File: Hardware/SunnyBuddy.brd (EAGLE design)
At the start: 47 x 47 mm, 38 parts, among them J1 5.5x2.1mm Barrel, J2 POWER_JACKPTH, J5 M02PTH, J6 M023.5MM, J7 M023.5MM, J8 M023.5MM, U1 LT3652

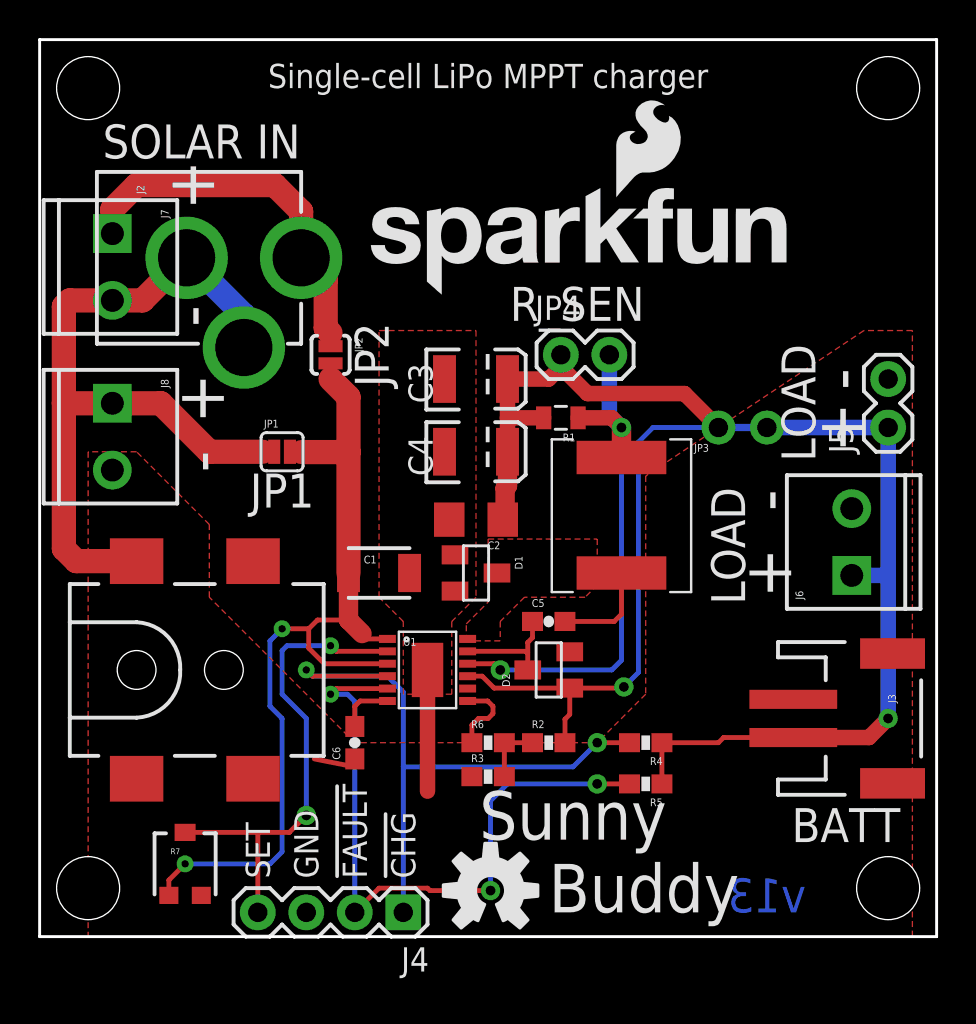
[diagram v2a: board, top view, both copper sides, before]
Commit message: added board fiducials
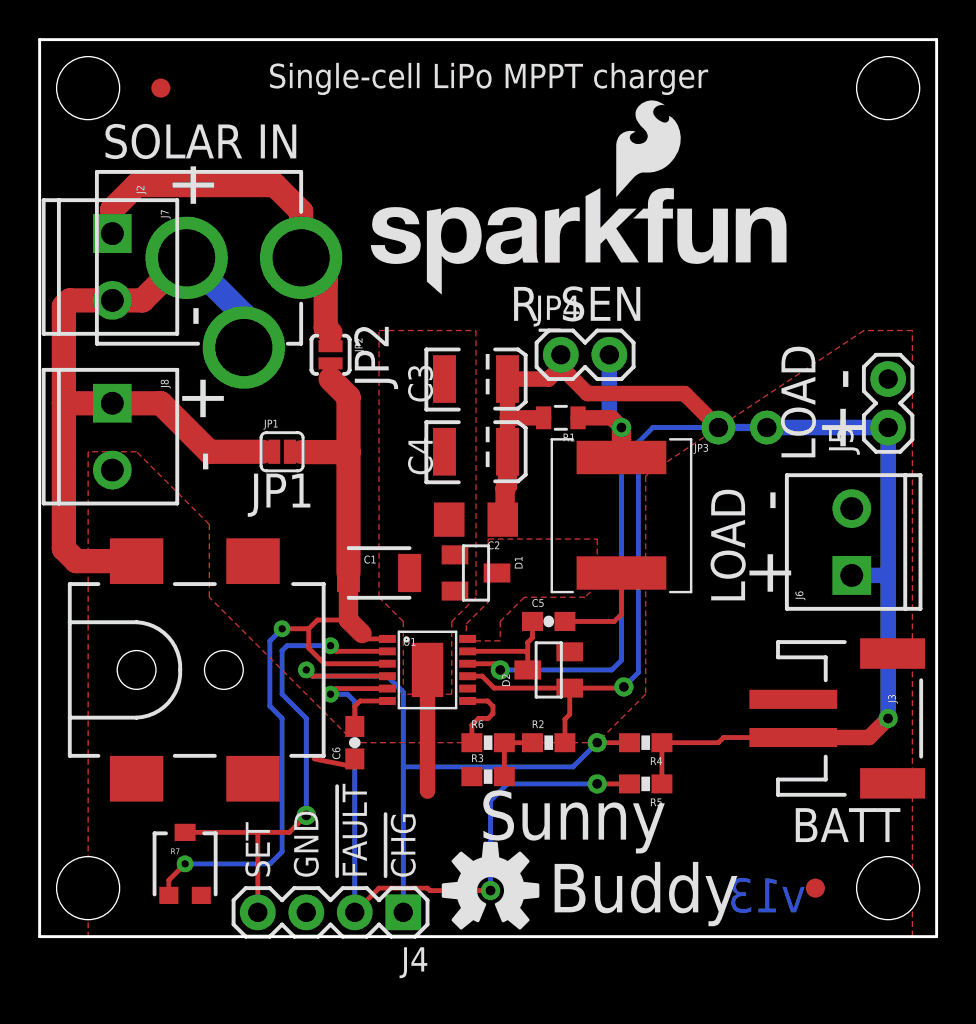
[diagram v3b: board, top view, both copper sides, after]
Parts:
- added FID1, FID2: FIDUCIAL1X2, SparkFun-Aesthetics:FIDUCIAL-1X2
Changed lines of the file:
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@@
 <?xml version="1.0" encoding="utf-8"?>
 <!DOCTYPE eagle SYSTEM "eagle.dtd">
-<eagle version="6.5.0">
+<eagle version="6.6.0">
 <drawing>
 <settings>
@@
 <setting verticaltext="up"/>
 </settings>
-<grid distance="0.05" unitdist="inch" unit="inch" style="lines" multiple="1" display="yes" altdistance="0.005" altunitdist="inch" altunit="inch"/>
+<grid distance="0.05" unitdist="inch" unit="inch" style="lines" multiple="1" display="yes" altdistance="0.01" altunitdist="inch" altunit="inch"/>
 <layers>
-<layer number="1" name="Top" color="4" fill="1" visible="no" active="yes"/>
-<layer number="2" name="Route2" color="1" fill="3" visible="no" active="yes"/>
-<layer number="15" name="Route15" color="4" fill="6" visible="no" active="yes"/>
+<layer number="1" name="Top" color="4" fill="1" visible="yes" active="yes"/>
+<layer number="2" name="Route2" color="1" fill="3" visible="yes" active="yes"/>
+<layer number="15" name="Route15" color="4" fill="6" visible="yes" active="yes"/>
 <layer number="16" name="Bottom" color="1" fill="1" visible="yes" active="yes"/>
 <layer number="17" name="Pads" color="2" fill="1" visible="yes" active="yes"/>
 <layer number="18" name="Vias" color="2" fill="1" visible="yes" active="yes"/>
 <layer number="19" name="Unrouted" color="6" fill="1" visible="yes" active="yes"/>
-<layer number="20" name="Dimension" color="15" fill="1" visible="yes" active="yes"/>
-<layer number="21" name="tPlace" color="16" fill="1" visible="no" active="yes"/>
-<layer number="22" name="bPlace" color="14" fill="1" visible="yes" active="yes"/>
-<layer number="23" name="tOrigins" color="15" fill="1" visible="no" active="yes"/>
+<layer number="20" name="Dimension" color="6" fill="1" visible="yes" active="yes"/>
+<layer number="21" name="tPlace" color="6" fill="1" visible="yes" active="yes"/>
+<layer number="22" name="bPlace" color="6" fill="1" visible="yes" active="yes"/>
+<layer number="23" name="tOrigins" color="15" fill="1" visible="yes" active="yes"/>
 <layer number="24" name="bOrigins" color="15" fill="1" visible="yes" active="yes"/>
-<layer number="25" name="tNames" color="7" fill="1" visible="no" active="yes"/>
-<layer number="26" name="bNames" color="7" fill="1" visible="no" active="yes"/>
-<layer number="27" name="tValues" color="7" fill="1" visible="no" active="yes"/>
-<layer number="28" name="bValues" color="7" fill="1" visible="no" active="yes"/>
-<layer number="29" name="tStop" color="7" fill="3" visible="no" active="yes"/>
-<layer number="30" name="bStop" color="7" fill="6" visible="no" active="yes"/>
-<layer number="31" name="tCream" color="7" fill="4" visible="no" active="yes"/>
-<layer number="32" name="bCream" color="7" fill="5" visible="no" active="yes"/>
-<layer number="39" name="tKeepout" color="4" fill="11" visible="no" active="yes"/>
-<layer number="40" name="bKeepout" color="1" fill="11" visible="no" active="yes"/>
-<layer number="41" name="tRestrict" color="4" fill="10" visible="no" active="yes"/>
-<layer number="42" name="bRestrict" color="1" fill="10" visible="no" active="yes"/>
-<layer number="43" name="vRestrict" color="2" fill="10" visible="no" active="yes"/>
-<layer number="44" name="Drills" color="7" fill="1" visible="no" active="yes"/>
-<layer number="45" name="Holes" color="7" fill="1" visible="no" active="yes"/>
-<layer number="46" name="Milling" color="3" fill="1" visible="no" active="yes"/>
-<layer number="51" name="tDocu" color="6" fill="1" visible="no" active="yes"/>
-<layer number="52" name="bDocu" color="7" fill="1" visible="no" active="yes"/>
+<layer number="25" name="tNames" color="7" fill="1" visible="yes" active="yes"/>
+<layer number="26" name="bNames" color="7" fill="1" visible="yes" active="yes"/>
+<layer number="27" name="tValues" color="7" fill="1" visible="yes" active="yes"/>
+<layer number="28" name="bValues" color="7" fill="1" visible="yes" active="yes"/>
+<layer number="29" name="tStop" color="7" fill="3" visible="yes" active="yes"/>
+<layer number="30" name="bStop" color="7" fill="6" visible="yes" active="yes"/>
+<layer number="31" name="tCream" color="7" fill="4" visible="yes" active="yes"/>
+<layer number="32" name="bCream" color="7" fill="5" visible="yes" active="yes"/>
+<layer number="39" name="tKeepout" color="4" fill="11" visible="yes" active="yes"/>
+<layer number="40" name="bKeepout" color="1" fill="11" visible="yes" active="yes"/>
+<layer number="41" name="tRestrict" color="4" fill="10" visible="yes" active="yes"/>
+<layer number="42" name="bRestrict" color="1" fill="10" visible="yes" active="yes"/>
+<layer number="43" name="vRestrict" color="2" fill="10" visible="yes" active="yes"/>
+<layer number="44" name="Drills" color="7" fill="1" visible="yes" active="yes"/>
+<layer number="45" name="Holes" color="7" fill="1" visible="yes" active="yes"/>
+<layer number="46" name="Milling" color="3" fill="1" visible="yes" active="yes"/>
+<layer number="51" name="tDocu" color="6" fill="1" visible="yes" active="yes"/>
+<layer number="52" name="bDocu" color="7" fill="1" visible="yes" active="yes"/>
 <layer number="3" name="Route3" color="4" fill="3" visible="no" active="no"/>
 <layer number="4" name="Route4" color="1" fill="4" visible="no" active="no"/>
@@
 <element name="LOGO3" library="SparkFun-Aesthetics" package="OSHW-LOGO-S" value="OSHW-LOGOS" x="2.54" y="7.62" rot="MR0"/>
 <element name="LOGO4" library="SparkFun-Aesthetics" package="SFE_LOGO_NAME_FLAME_.3" value="SFE_LOGO_NAME_FLAME.3_INCH" x="40.64" y="15.24" rot="MR0"/>
+<element name="FID1" library="SparkFun-Aesthetics" package="FIDUCIAL-1X2" value="FIDUCIAL1X2" x="6.35" y="44.45"/>
+<element name="FID2" library="SparkFun-Aesthetics" package="FIDUCIAL-1X2" value="FIDUCIAL1X2" x="40.64" y="2.54"/>
 </elements>
 <signals>
